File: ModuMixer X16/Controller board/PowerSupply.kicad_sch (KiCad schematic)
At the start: 46 parts, among them J7 Screw_Terminal_01x02, K1 Relay_SPST_Latching_1coil, Q2 MMBT2222A, SW22 SW_SPST, U3 LM317_TO-220, U4 LM317_TO-220, U5 LM317_TO-220

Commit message: update idk
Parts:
- renumbered C22 to C21, C23 to C22, C24 to C23, C25 to C24, C26 to C25, C27 to C26, C28 to C27, C29 to C28, C30 to C29, C31 to C30, C32 to C31, C33 to C32, C34 to C33, C35 to C34, C36 to C35, C37 to C36, C38 to C37, J7 to J6, U3 to U2, U4 to U3, U5 to U4

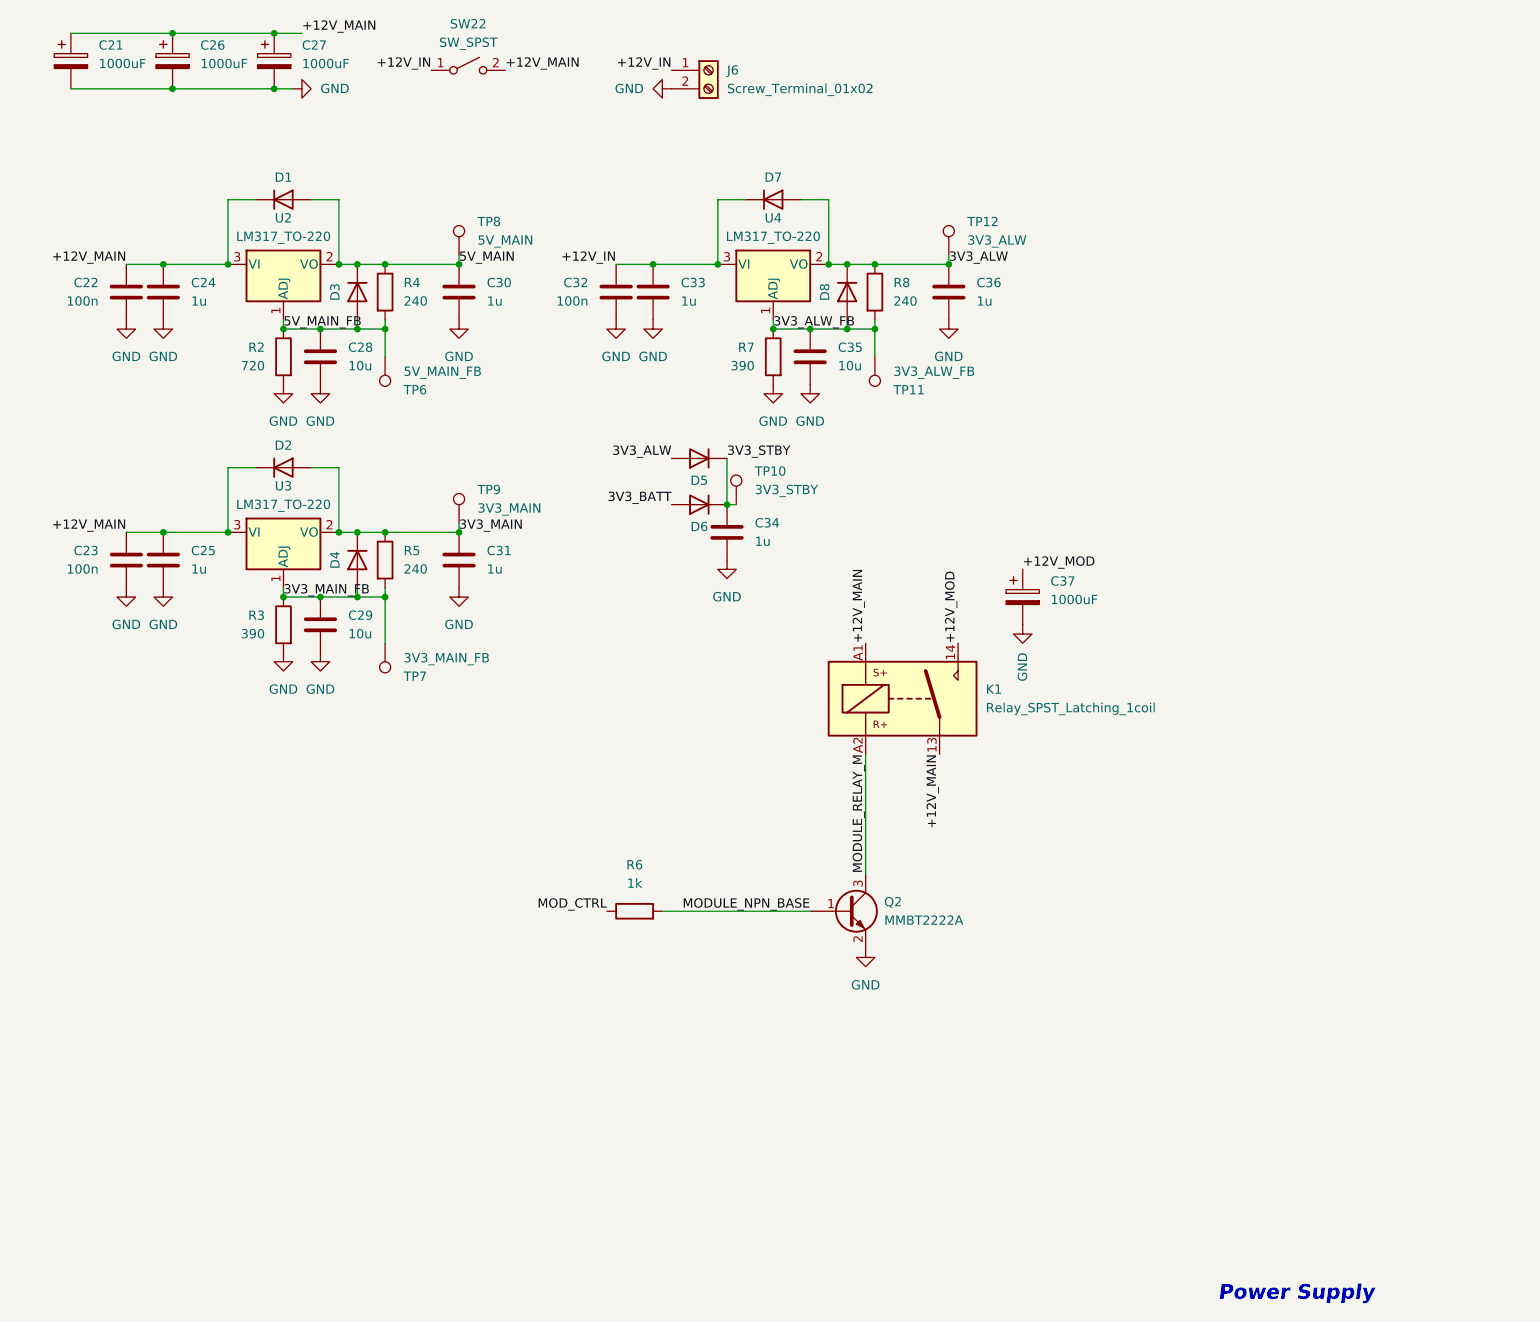
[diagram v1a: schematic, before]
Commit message: Midway through MCU replacement
Sometimes i feel like it would be better to start over considering it's a digital mixer.
The only thing left is doing the DSP connections and calculating the values for a 16mhz crystal on all 3 MCUs
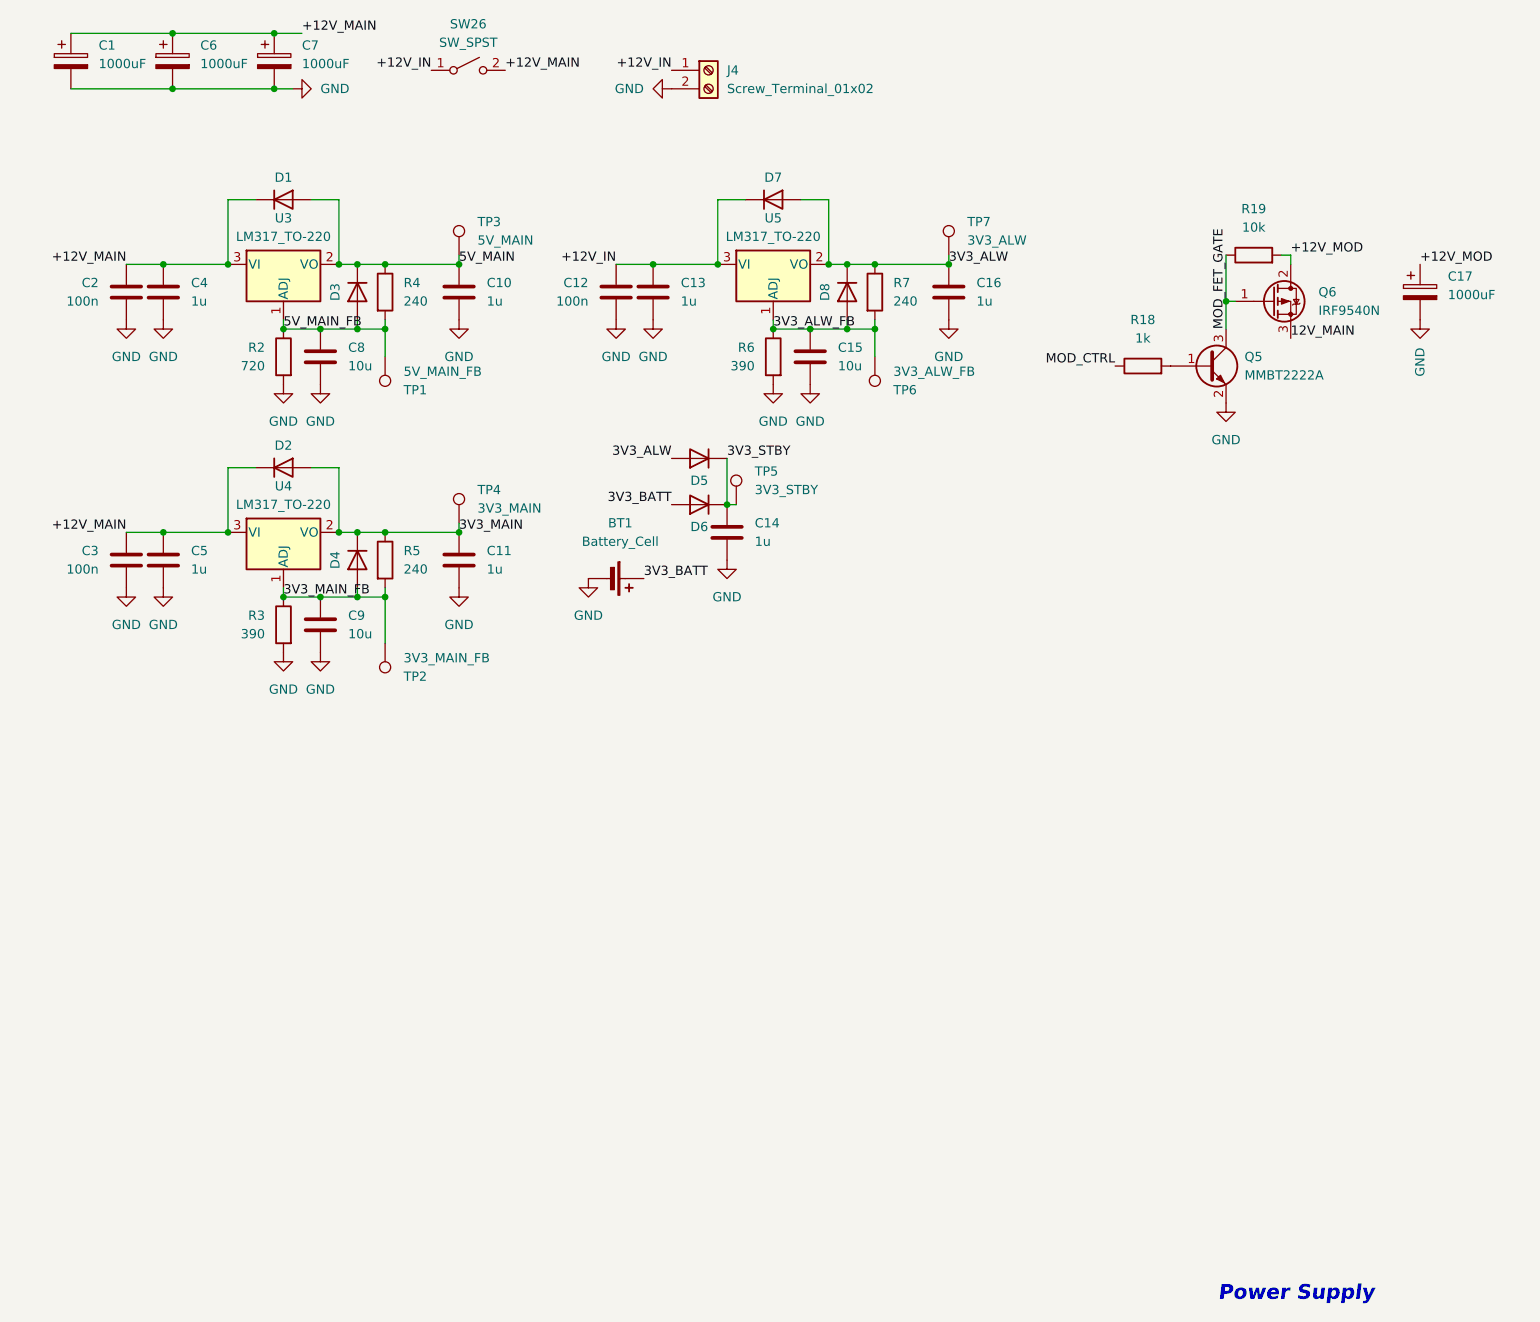
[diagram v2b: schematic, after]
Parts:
- removed K1: Relay_SPST_Latching_1coil, Relay_THT:Relay_SPST_Zettler-AZSR131, symbol Relay:Relay_SPST_Latching_1coil
- removed Q2: MMBT2222A, Package_TO_SOT_SMD:SOT-23, symbol Transistor_BJT:MMBT2222A
- removed R6: 1k, Resistor_SMD:R_0603_1608Metric, symbol Device:R
- added BT1: Battery_Cell, symbol Device:Battery_Cell
- added Q5: MMBT2222A, Package_TO_SOT_SMD:SOT-23, symbol Transistor_BJT:MMBT2222A
- added Q6: IRF9540N, Package_TO_SOT_THT:TO-220-3_Vertical, symbol Transistor_FET:IRF9540N
- added R18: 1k, symbol Device:R
- added R19: 10k, symbol Device:R
- renumbered C21 to C1, C30 to C10, C31 to C11, C32 to C12, C33 to C13, C34 to C14, C35 to C15, C36 to C16, C37 to C17, C22 to C2, C23 to C3, C24 to C4, C25 to C5, C26 to C6, C27 to C7, C28 to C8, C29 to C9, J6 to J4, R7 to R6, R8 to R7, SW22 to SW26, TP6 to TP1, TP7 to TP2, TP8 to TP3, TP9 to TP4, TP10 to TP5, TP11 to TP6, TP12 to TP7, U2 to U3, U3 to U4, U4 to U5
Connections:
- net +12V_MOD: now also Q6.2 (D), R19.2
- net 3V3_BATT: now also BT1.1 (+)
- net GND: now also BT1.2 (-), Q5.2 (E)
- net MOD_CTRL: now also R18.1
- new net: Q5.1 (B), R18.2
- new net 12V_MAIN: Q6.3 (S)
- new net MOD_FET_GATE: Q5.3 (C), Q6.1 (G), R19.1
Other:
- moved on the sheet: C17

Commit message: asdasgashg
sfjhadgdjasdg
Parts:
- removed TP3: 5V_MAIN, TestPoint:TestPoint_Pad_D3.0mm, symbol Connector:TestPoint
- removed TP4: 3V3_MAIN, TestPoint:TestPoint_Pad_D3.0mm, symbol Connector:TestPoint
- removed TP5: 3V3_STBY, TestPoint:TestPoint_Pad_D3.0mm, symbol Connector:TestPoint
- removed TP7: 3V3_ALW, TestPoint:TestPoint_Pad_D3.0mm, symbol Connector:TestPoint
- R11: renamed from R18; footprint (none) -> Resistor_SMD:R_0603_1608Metric
- R12: renamed from R19; footprint (none) -> Resistor_SMD:R_0603_1608Metric
- renumbered C1 to C17, C2 to C18, C3 to C19, C4 to C20, C5 to C21, C6 to C22, C7 to C23, C8 to C24, C9 to C25, C10 to C26, C11 to C27, C12 to C28, C13 to C29, C14 to C30, C15 to C31, C16 to C32, C17 to C33, J4 to J6, Q5 to Q2, Q6 to Q3, R7 to R10, R2 to R5, R3 to R6, R4 to R7, R5 to R8, R6 to R9
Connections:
- net +12V_MOD: no longer Q3.2 (D), R12.2
- net 12V_MAIN: now also Q3.2 (D), R12.2; no longer Q3.3 (S)
- new net 12V_MOD: Q3.3 (S)

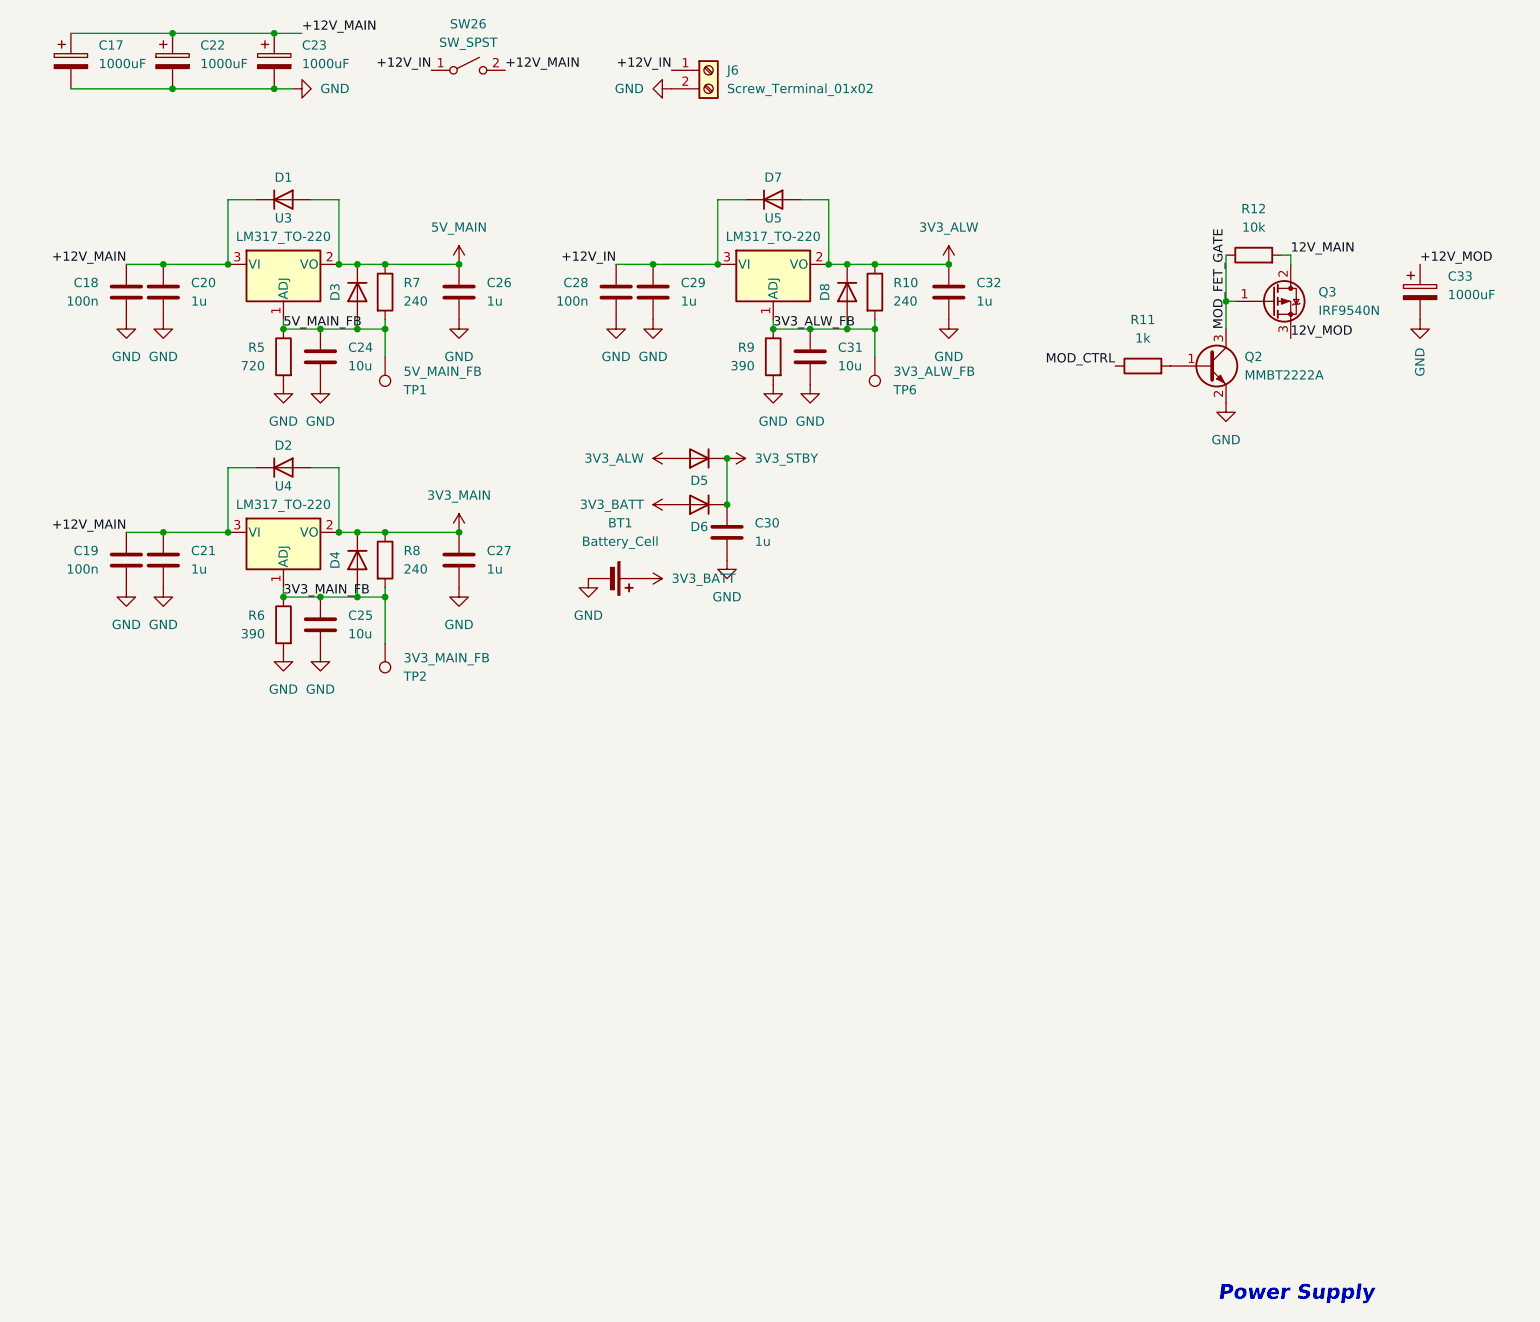
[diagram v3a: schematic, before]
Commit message: Changed all labels to global
I made it in a rather hacky way (editing all files on notepad with Ctrl + H), i'm only reverting this if something breaks
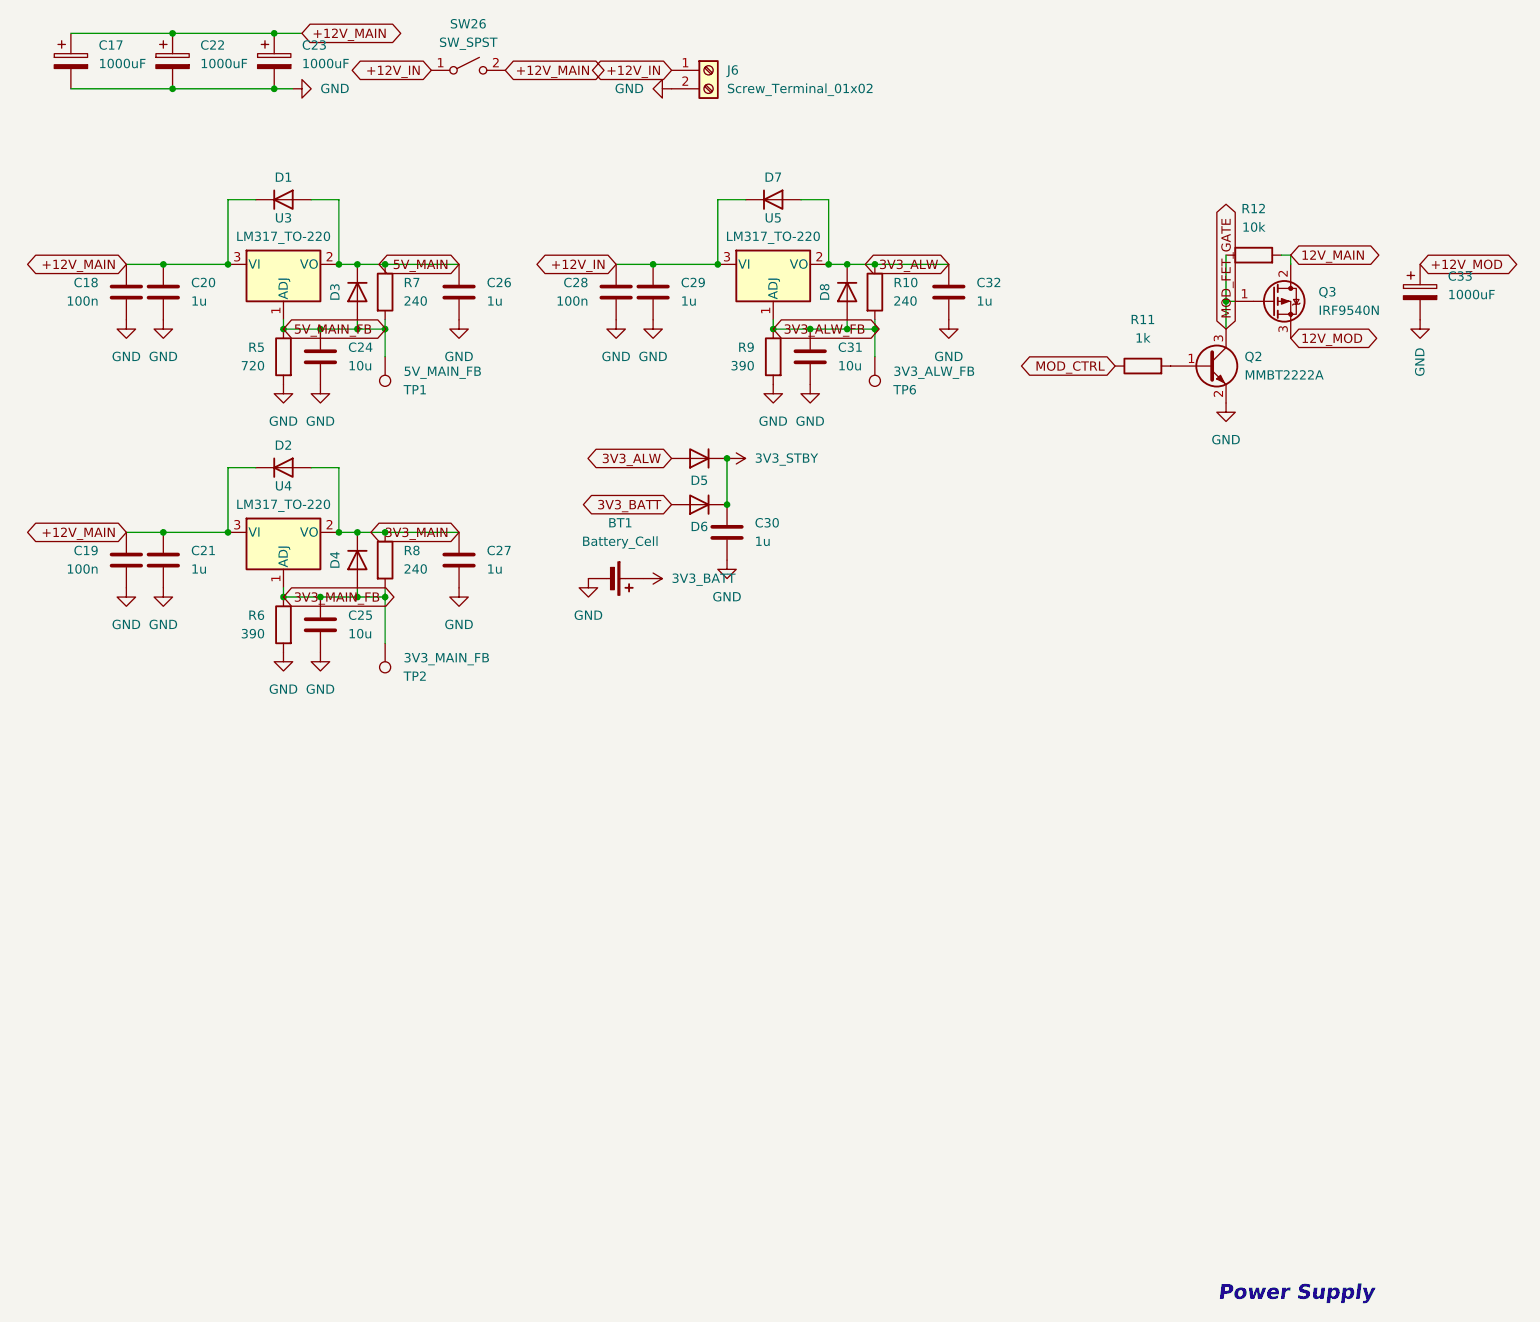
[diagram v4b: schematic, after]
